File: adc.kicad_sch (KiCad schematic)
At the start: 17 parts, among them U8 TLA2518IRTER

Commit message: did stuff
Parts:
- removed C77: C, symbol Device:C
- removed D36, D37: D, symbol Device:D
- removed R67: R, symbol Device:R
- added D47, D48, D49, D50, D51, D52, D53, D54: BAS40-04, Package_TO_SOT_SMD:SOT-23, symbol Diode:BAS40-04
- U8: footprint WQFN16_RTE_TEX -> (none)
- renumbered C53 to C115, C51 to C116, C52 to C117, TP104 to TP136, TP105 to TP137, TP106 to TP138, TP107 to TP139, TP108 to TP140, TP109 to TP141, TP110 to TP142, TP111 to TP143, TP136 to TP144
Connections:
- net +VADC: now also D47.2, D48.2, D49.2, D50.2, D51.2, D52.2, D53.2, D54.2
- net GND: now also D47.1, D48.1, D49.1, D50.1, D51.1, D52.1, D53.1, D54.1
- net GPIO0: now also D50.3
- net GPIO1: now also D54.3
- net GPIO2: now also D49.3
- net GPIO3: now also D53.3
- net GPIO4: now also D48.3
- net GPIO5: now also D52.3
- net GPIO6: now also D47.3
- net GPIO7: now also D51.3
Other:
- moved on the sheet: C115, C116, C117, TP136, TP137, TP138, TP139, TP140, TP141, TP142, TP143, TP144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

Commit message: changed to 4 layer, finished usb conn, added jtag conn, some other things
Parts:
- TP136, TP137, TP138, TP139, TP140, TP141, TP142, TP143: footprint (none) -> TestPoint:TestPoint_THTPad_D1.0mm_Drill0.5mm
- TP144: footprint (none) -> TestPoint:TestPoint_THTPad_1.0x1.0mm_Drill0.5mm
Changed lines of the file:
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@@
 			)
 		)
-		(property "Footprint" ""
+		(property "Footprint" "TestPoint:TestPoint_THTPad_D1.0mm_Drill0.5mm"
 			(at 123.19 80.01 0)
 			(hide yes)
@@
 			)
 		)
-		(property "Footprint" ""
+		(property "Footprint" "TestPoint:TestPoint_THTPad_1.0x1.0mm_Drill0.5mm"
 			(at 118.11 132.08 0)
 			(hide yes)
@@
 			)
 		)
-		(property "Footprint" ""
+		(property "Footprint" "TestPoint:TestPoint_THTPad_D1.0mm_Drill0.5mm"
 			(at 123.19 87.63 0)
 			(hide yes)
@@
 			)
 		)
-		(property "Footprint" ""
+		(property "Footprint" "TestPoint:TestPoint_THTPad_D1.0mm_Drill0.5mm"
 			(at 123.19 92.71 0)
 			(hide yes)
@@
 			)
 		)
-		(property "Footprint" ""
+		(property "Footprint" "TestPoint:TestPoint_THTPad_D1.0mm_Drill0.5mm"
 			(at 123.19 82.55 0)
 			(hide yes)
@@
 			)
 		)
-		(property "Footprint" ""
+		(property "Footprint" "TestPoint:TestPoint_THTPad_D1.0mm_Drill0.5mm"
 			(at 123.19 85.09 0)
 			(hide yes)
@@
 			)
 		)
-		(property "Footprint" ""
+		(property "Footprint" "TestPoint:TestPoint_THTPad_D1.0mm_Drill0.5mm"
 			(at 123.19 97.79 0)
 			(hide yes)
@@
 			)
 		)
-		(property "Footprint" ""
+		(property "Footprint" "TestPoint:TestPoint_THTPad_D1.0mm_Drill0.5mm"
 			(at 123.19 90.17 0)
 			(hide yes)
@@
 			)
 		)
-		(property "Footprint" ""
+		(property "Footprint" "TestPoint:TestPoint_THTPad_D1.0mm_Drill0.5mm"
 			(at 123.19 95.25 0)
 			(hide yes)

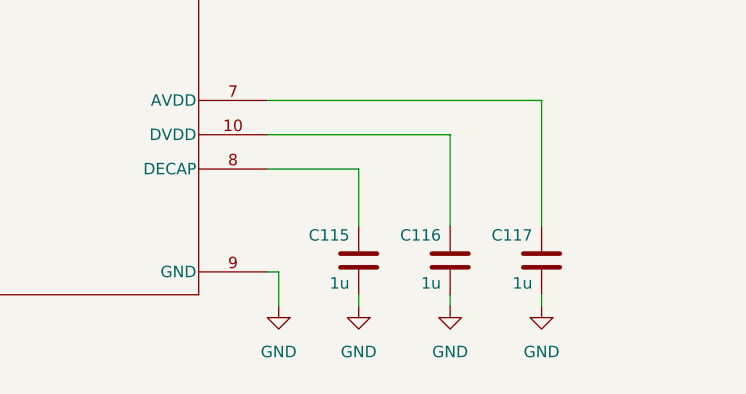
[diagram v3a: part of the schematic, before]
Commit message: did a bunch of bom matching to lcsc
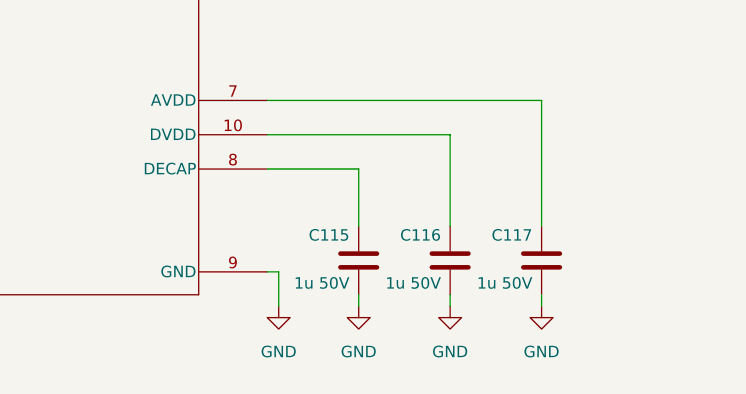
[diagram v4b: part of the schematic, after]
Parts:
- C115, C116, C117: value 1u -> 1u 50V; LCSC (none) -> C15849; LCSC Basic/Pref (none) -> x; LCSC Part (none) -> C15849
- D47, D48, D49, D50, D51, D52, D53, D54: LCSC Part (none) -> C142620
- TP136, TP137, TP138, TP139, TP140, TP141, TP142, TP143, TP144: now left out of the parts list
- U8: LCSC Part (none) -> C1855741

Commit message: bunch of stuff
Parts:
- U8: footprint (none) -> TLA2518IRTER:WQFN16_RTE_TEX
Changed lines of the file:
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@@
 			)
 		)
-		(property "Footprint" ""
+		(property "Footprint" "TLA2518IRTER:WQFN16_RTE_TEX"
 			(at 124.46 72.39 0)
 			(hide yes)
